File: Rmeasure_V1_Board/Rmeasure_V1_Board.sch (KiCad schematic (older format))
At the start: 52 parts, among them J1 USB_C_Receptacle_USB2.0, J2 CON_debug, J3 Conn_ARM_JTAG_SWD_10, J4 CON_CAN, J5 CON_CAN, SW1 BOOT, SW2 RST, U1 STM32F302C6Tx, U2 NCP1117-3.3_SOT223, U3 SN65HVD232, Y1 8MHz

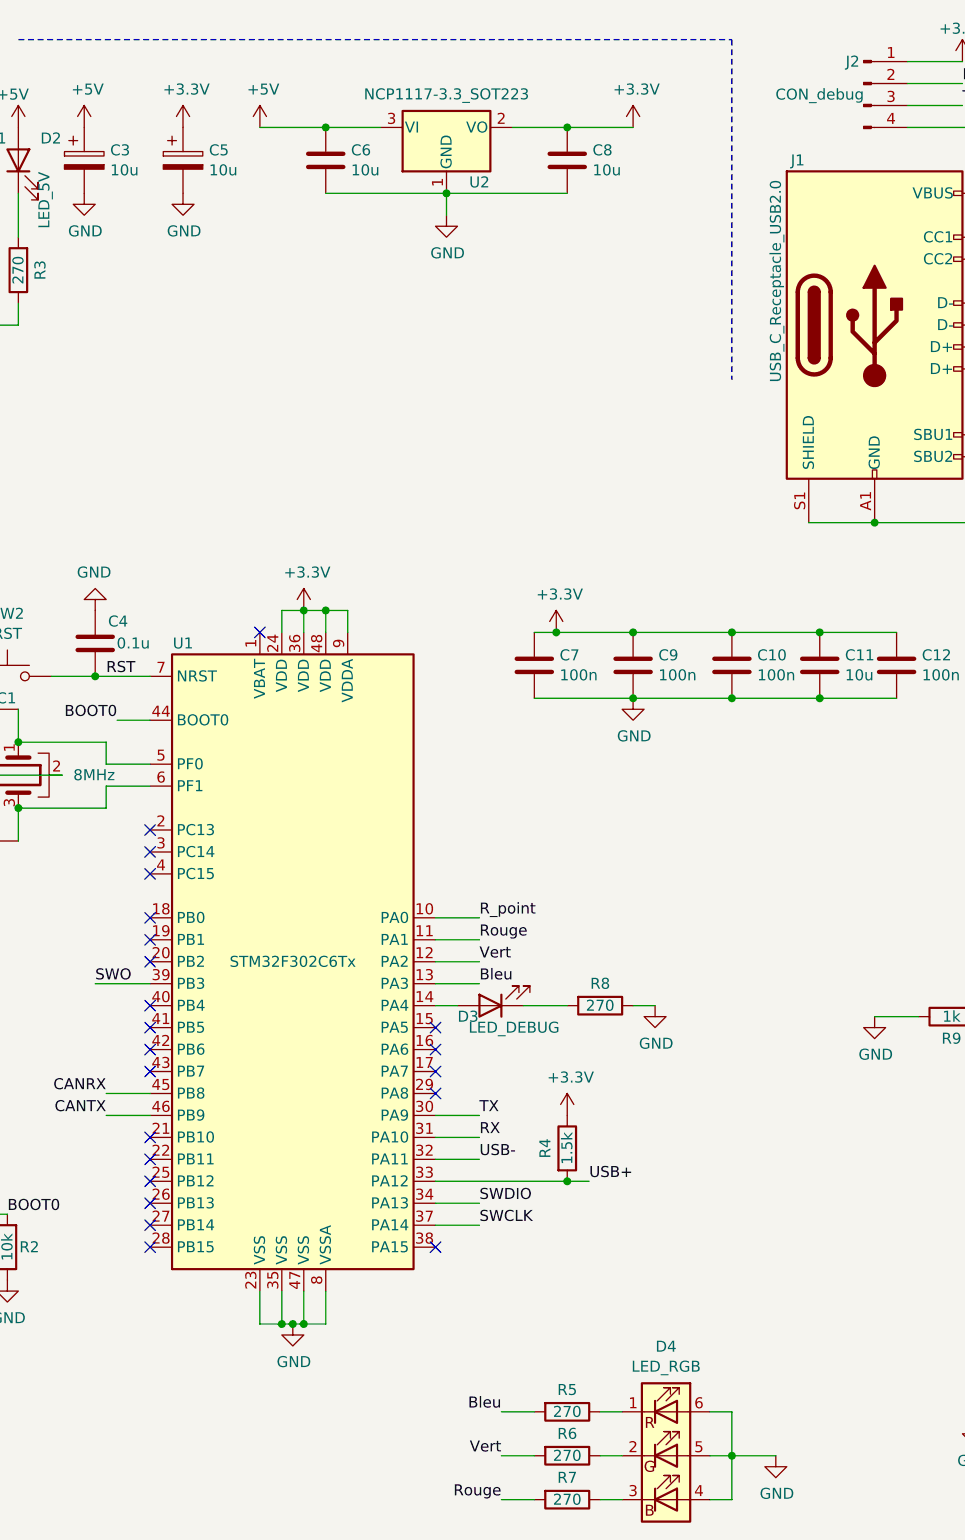
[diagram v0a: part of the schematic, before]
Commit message: IO prete, Pompe finir sérigraphie, Alim+AX12 à faire
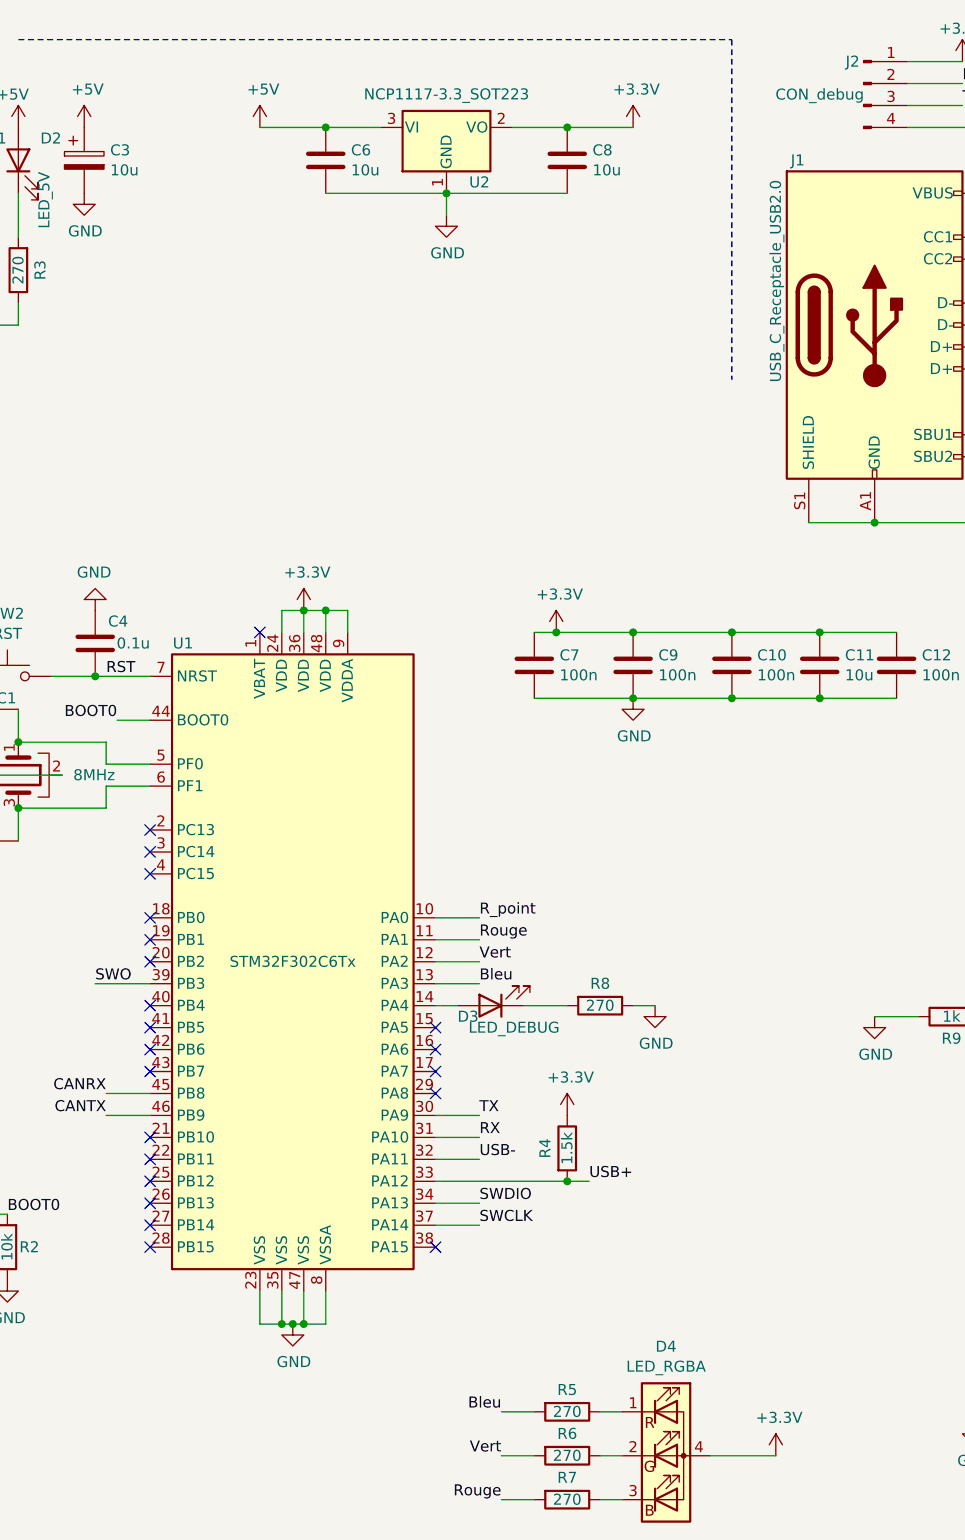
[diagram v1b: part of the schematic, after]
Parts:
- removed C5: 10u, Capacitor_THT:CP_Radial_D4.0mm_P2.00mm, symbol Device:CP
- removed D4: LED_RGB, AREA_lib_composant:LED_RGB_LTRBRASF6B6C011200R18, symbol Device:LED_RGB
- added D4: LED_RGBA, LED_SMD:LED_SK6812_EC15_1.5x1.5mm, symbol Device:LED_RGBA
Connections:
- net +3V3: now also D4.4 (A)
- net at R5.1: now also D4.1 (RK)
- net at R6.1: now also D4.2 (GK)
- net at R7.1: now also D4.3 (BK)
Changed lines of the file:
@@
-$EndComp
-$Comp
-L power:+3.3V #PWR011
-U 1 1 6158E83C
-P 2000 1100
-F 0 "#PWR011" H 2000 950 50  0001 C CNN
-F 1 "+3.3V" H 2015 1273 50  0000 C CNN
-F 2 "" H 2000 1100 50  0001 C CNN
-F 3 "" H 2000 1100 50  0001 C CNN
-	1    2000 1100
-	1    0    0    -1
 $EndComp
 $Comp
@@
 $EndComp
 $Comp
-L Device:CP C5
-U 1 1 6158F65D
-P 2000 1250
-F 0 "C5" H 2118 1296 50  0000 L CNN
-F 1 "10u" H 2118 1205 50  0000 L CNN
-F 2 "Capacitor_THT:CP_Radial_D4.0mm_P2.00mm" H 2038 1100 50  0001 C CNN
-F 3 "~" H 2000 1250 50  0001 C CNN
-	1    2000 1250
-	1    0    0    -1
-$EndComp
-$Comp
 L power:GND #PWR09
 U 1 1 6158FEC2
@@
 F 3 "" H 1550 1400 50  0001 C CNN
 	1    1550 1400
-	1    0    0    -1
-$EndComp
-$Comp
-L power:GND #PWR012
-U 1 1 6159025E
-P 2000 1400
-F 0 "#PWR012" H 2000 1150 50  0001 C CNN
-F 1 "GND" H 2005 1227 50  0000 C CNN
-F 2 "" H 2000 1400 50  0001 C CNN
-F 3 "" H 2000 1400 50  0001 C CNN
-	1    2000 1400
 	1    0    0    -1
 $EndComp
@@
 Text Label 3450 6950 2    50   ~ 0
 Bleu
-Wire Wire Line
-	4500 7150 4700 7150
 Wire Wire Line
 	9200 1300 9450 1300
@@
 NoConn ~ 3150 6200
 $Comp
-L Device:LED_RGB D4
-U 1 1 6180651B
+L Device:LED_RGBA D4
+U 1 1 619DE875
 P 4200 7150
 F 0 "D4" H 4200 7647 50  0000 C CNN
-F 1 "LED_RGB" H 4200 7556 50  0000 C CNN
-F 2 "AREA_lib_composant:LED_RGB_LTRBRASF6B6C011200R18" H 4200 7100 50  0001 C CNN
+F 1 "LED_RGBA" H 4200 7556 50  0000 C CNN
+F 2 "LED_SMD:LED_SK6812_EC15_1.5x1.5mm" H 4200 7100 50  0001 C CNN
 F 3 "~" H 4200 7100 50  0001 C CNN
 	1    4200 7150
@@
 $EndComp
 Wire Wire Line
-	4400 6950 4500 6950
-Wire Wire Line
-	4500 6950 4500 7150
-Wire Wire Line
-	4500 7150 4500 7350
-Wire Wire Line
-	4500 7350 4400 7350
-Connection ~ 4500 7150
-Wire Wire Line
-	4400 7150 4500 7150
-$Comp
-L power:GND #PWR0101
-U 1 1 6185EE35
+	4400 7150 4700 7150
+$Comp
+L power:+3.3V #PWR023
+U 1 1 619E28FA
 P 4700 7150
-F 0 "#PWR0101" H 4700 6900 50  0001 C CNN
-F 1 "GND" H 4705 6977 50  0000 C CNN
+F 0 "#PWR023" H 4700 7000 50  0001 C CNN
+F 1 "+3.3V" H 4715 7323 50  0000 C CNN
 F 2 "" H 4700 7150 50  0001 C CNN
 F 3 "" H 4700 7150 50  0001 C CNN
